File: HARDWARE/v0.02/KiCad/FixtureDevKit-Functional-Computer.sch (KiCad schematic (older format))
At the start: 12 parts, among them J15 Conn_01x20, J16 Conn_01x20, J17 CHIP4RH, J20 Conn_01x20, J21 Conn_01x20, J23 CHIP4LH, J25 JST-2P-RA, SW5 YSS-19-1202-N, SW6 TL9210AF260Q

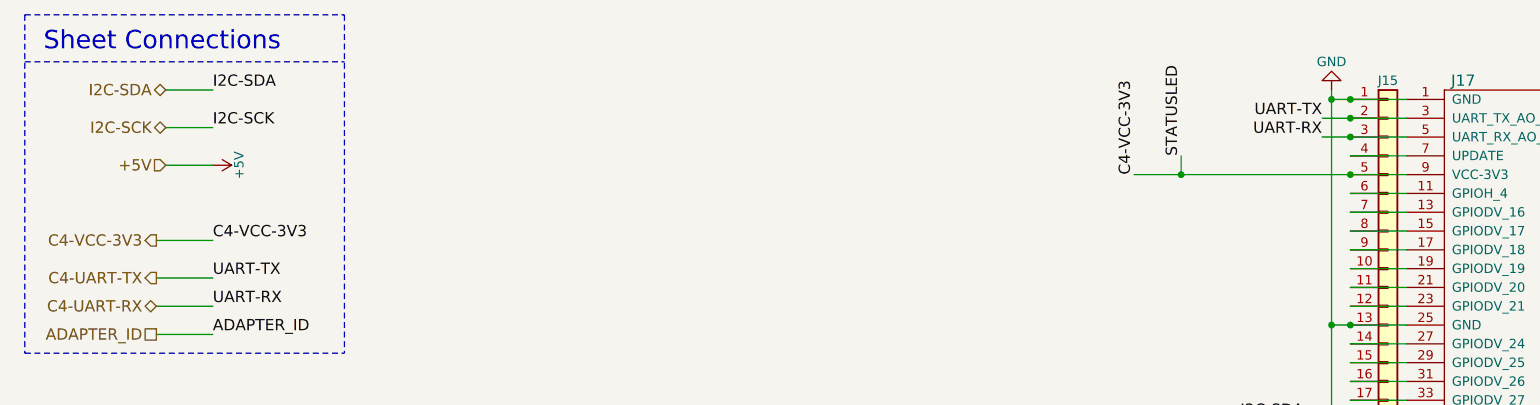
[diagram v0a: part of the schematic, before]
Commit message: adding latest updates from pcb layout designed 11/8/2017
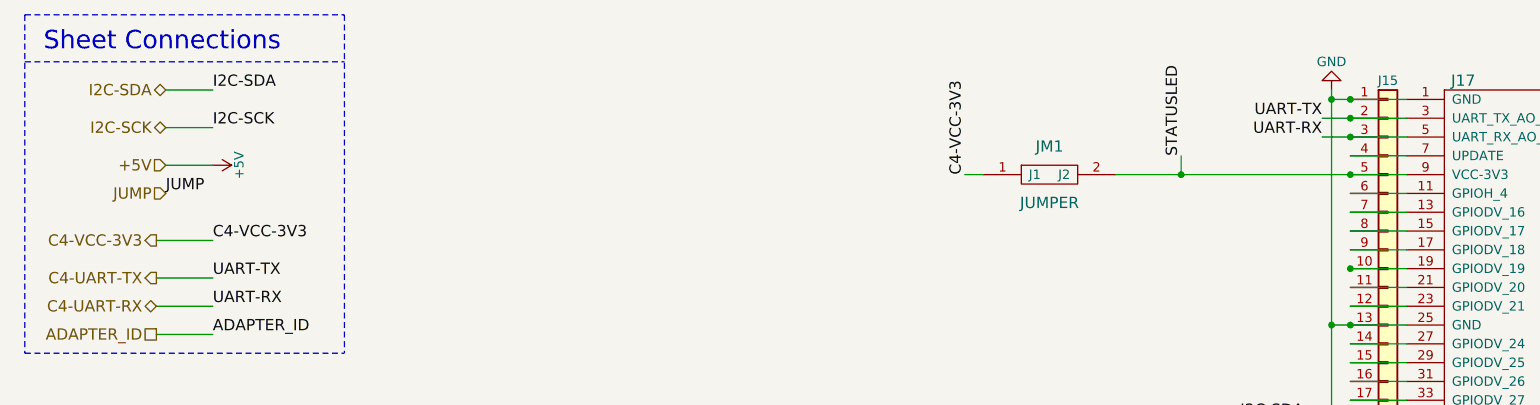
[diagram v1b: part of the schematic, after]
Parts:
- added JM1: JUMPER, Jumper:Jumper, symbol JUMPER
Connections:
- net C4-VCC-3V3: now also JM1.1 (J1); no longer D9.2 (A), J15.5 (Pin_5), J17.9 (VCC-3V3)
- new net STATUSLED: D9.2 (A), J15.5 (Pin_5), J17.9 (VCC-3V3), JM1.2 (J2)
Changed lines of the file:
@@
 LIBS:TCA6424ARGJR
 LIBS:USB-A1HSW6
+LIBS:jumper
 LIBS:Fixture-Dev-Kit-cache
 EELAYER 25 0
@@
 $EndComp
 $Comp
-L GND #PWR18
+L GND #PWR25
 U 1 1 59EE7DE0
 P 7450 900
-F 0 "#PWR18" H 7450 650 50  0001 C CNN
+F 0 "#PWR25" H 7450 650 50  0001 C CNN
 F 1 "GND" H 7450 750 50  0000 C CNN
 F 2 "" H 7450 900 50  0001 C CNN
@@
 $EndComp
 $Comp
-L GND #PWR19
+L GND #PWR27
 U 1 1 59EE7F13
 P 9800 900
-F 0 "#PWR19" H 9800 650 50  0001 C CNN
+F 0 "#PWR27" H 9800 650 50  0001 C CNN
 F 1 "GND" H 9800 750 50  0000 C CNN
 F 2 "" H 9800 900 50  0001 C CNN
@@
 $EndComp
 $Comp
-L GND #PWR21
+L GND #PWR26
 U 1 1 59EE8282
 P 7450 3600
-F 0 "#PWR21" H 7450 3350 50  0001 C CNN
+F 0 "#PWR26" H 7450 3350 50  0001 C CNN
 F 1 "GND" H 7450 3450 50  0000 C CNN
 F 2 "" H 7450 3600 50  0001 C CNN
@@
 $EndComp
 $Comp
-L GND #PWR22
+L GND #PWR28
 U 1 1 59EE829F
 P 9800 3600
-F 0 "#PWR22" H 9800 3350 50  0001 C CNN
+F 0 "#PWR28" H 9800 3350 50  0001 C CNN
 F 1 "GND" H 9800 3450 50  0000 C CNN
 F 2 "" H 9800 3600 50  0001 C CNN
@@
 $EndComp
 $Comp
-L GND #PWR27
+L GND #PWR22
 U 1 1 59EE95A1
 P 1900 7450
-F 0 "#PWR27" H 1900 7200 50  0001 C CNN
+F 0 "#PWR22" H 1900 7200 50  0001 C CNN
 F 1 "GND" H 1900 7300 50  0000 C CNN
 F 2 "" H 1900 7450 50  0001 C CNN
@@
 $EndComp
 $Comp
-L GND #PWR26
+L GND #PWR20
 U 1 1 59EEA1C1
 P 900 7450
-F 0 "#PWR26" H 900 7200 50  0001 C CNN
+F 0 "#PWR20" H 900 7200 50  0001 C CNN
 F 1 "GND" H 900 7300 50  0000 C CNN
 F 2 "" H 900 7450 50  0001 C CNN
@@
 $EndComp
 $Comp
-L GND #PWR25
+L GND #PWR23
 U 1 1 59EEADAD
 P 2650 7250
-F 0 "#PWR25" H 2650 7000 50  0001 C CNN
+F 0 "#PWR23" H 2650 7000 50  0001 C CNN
 F 1 "GND" H 2650 7100 50  0000 C CNN
 F 2 "" H 2650 7250 50  0001 C CNN
@@
 Sheet Connections
 $Comp
-L +5V #PWR20
+L +5V #PWR21
 U 1 1 59F1E155
 P 1500 1300
-F 0 "#PWR20" H 1500 1150 50  0001 C CNN
+F 0 "#PWR21" H 1500 1150 50  0001 C CNN
 F 1 "+5V" H 1500 1440 50  0000 C CNN
 F 2 "" H 1500 1300 50  0001 C CNN
@@
 +5V
 $Comp
-L +5V #PWR23
+L +5V #PWR19
 U 1 1 59F1EC3F
 P 800 4800
-F 0 "#PWR23" H 800 4650 50  0001 C CNN
+F 0 "#PWR19" H 800 4650 50  0001 C CNN
 F 1 "+5V" H 800 4940 50  0000 C CNN
 F 2 "" H 800 4800 50  0001 C CNN
@@
 Wire Wire Line
 	1200 1700 1500 1700
-Text Label 6400 1350 1    60   ~ 0
+Text Label 5500 1350 1    60   ~ 0
 C4-VCC-3V3
 Connection ~ 9700 3650
@@
 	700  5200 700  5250
 Wire Wire Line
-	6400 1350 7850 1350
+	6300 1350 7850 1350
 Wire Wire Line
 	6650 1350 6650 1250
@@
 Wire Notes Line
 	500  2300 2200 2300
+$Comp
+L JUMPER JM1
+U 1 1 5A02D707
+P 5950 1350
+F 0 "JM1" H 5950 1500 60  0000 C CNN
+F 1 "JUMPER" H 5950 1200 60  0000 C CNN
+F 2 "Jumper:Jumper" H 5950 1350 60  0001 C CNN
+F 3 "" H 5950 1350 60  0001 C CNN
+	1    5950 1350
+	1    0    0    -1
+$EndComp
+Connection ~ 7550 1850
+Text HLabel 1250 1450 0    60   Input ~ 0
+JUMP
+Text Label 1250 1450 0    60   ~ 0
+JUMP
+Wire Wire Line
+	5600 1350 5500 1350
 $EndSCHEMATC
